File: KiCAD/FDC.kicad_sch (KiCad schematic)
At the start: 26 parts, among them J2 Conn_02x20_Odd_Even, J3 SD_Card, Q1 SSM3K324RLFCT-ND, Q2 SSM3K324RLFCT-ND, U1 SN74LVCC4245ADWR, U2 Pico 2, U3 SN74LVCC4245ADWR, U4 SN74LVCC4245ADWR, U5 SN74LVCC4245ADWR

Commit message: First upload of test board.
First upload of test board.
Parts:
- removed C4, C5, C6, C7, C8: 100nF, Capacitor_SMD:C_0805_2012Metric_Pad1.18x1.45mm_HandSolder, symbol Device:C
- removed D2: PMEG4010CEJ, Diode_SMD:D_SOD-323F, symbol Diode:PMEG4010CEJ
- removed J2: Conn_02x20_Odd_Even, Connector_PinSocket_2.54mm:PinSocket_2x20_P2.54mm_Vertical, symbol Connector_Generic:Conn_02x20_Odd_Even
- removed J3: SD_Card, Connector_Card:SD_Kyocera_145638009511859+, symbol Connector:SD_Card
- removed R2: 1k, Resistor_SMD:R_0805_2012Metric_Pad1.20x1.40mm_HandSolder, symbol Device:R_US
- removed U1, U3, U4, U5: SN74LVCC4245ADWR, Package_SO:SOIC-24W_7.5x15.4mm_P1.27mm, symbol Logic_LevelTranslator:SN74AVC8T245PW
- added J1: Conn_01x04, Connector_PinHeader_2.54mm:PinHeader_1x04_P2.54mm_Vertical, symbol Connector_Generic:Conn_01x04
- added R1: 1k, Resistor_SMD:R_0805_2012Metric_Pad1.20x1.40mm_HandSolder, symbol Device:R_US
- added SDCARD1: ST-TF-003A, 00-ProjectLib:MicroSD_Card_TB, symbol MicroSDCardSlot:ST-TF-003A
- added U1, U2, U3: 74HCT245, Package_SO:SOIC-20W_7.5x15.4mm_P1.27mm, symbol 74xx:74HC245
- added U6, U7: Z80, Package_DIP:DIP-40_W15.24mm, symbol CPU:Z84C00xxP
- D1: footprint LED_SMD:LED_2816_7142Metric_Pad3.20x4.45mm_HandSolder -> LED_THT:LED_D5.0mm
- PICO2: renamed from U2; footprint MCU_RaspberryPi_and_Boards:RPi_Pico_SMD_TH -> Module:RaspberryPi_Pico_SMD
- Q1, Q2: value SSM3K324RLFCT-ND -> 2N7002; Digikey SSM3K324RLFCT-ND -> 2N7002NTR-ND
- renumbered C9 to C4, R3 to R2, R4 to R3, R6 to R4, R8 to R5, R1 to R6
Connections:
- net RD' is gone; now on net RD*: PICO2.15 (GPIO11)
- net WR' is gone; now on net WR*: PICO2.16 (GPIO12)
- net +3V3: now also R2.1, SDCARD1.4 (VDD); no longer C1.1, C2.1, R2.2
- net +5V: now also C1.1, C2.1, R1.2, U1.20 (VCC), U2.1 (A->B), U2.20 (VCC), U3.1 (A->B), U3.20 (VCC), U6.11 (V_{CC}), U7.11 (V_{CC})
- net A0: now also U2.9 (A7), U6.30 (A_{0}), U7.30 (A_{0})
- net A1: now also U2.8 (A6), U6.31 (A_{1}), U7.31 (A_{1})
- net A10: now also U3.7 (A5), U6.40 (A_{10}), U7.40 (A_{10})
- net A11: now also U3.6 (A4), U6.1 (A_{11}), U7.1 (A_{11})
- net A12: now also U3.2 (A0), U6.2 (A_{12}), U7.2 (A_{12})
- net A13: now also U3.3 (A1), U6.3 (A_{13}), U7.3 (A_{13})
- net A14: now also U3.4 (A2), U6.4 (A_{14}), U7.4 (A_{14})
- net A15: now also U3.5 (A3), U6.5 (A_{15}), U7.5 (A_{15})
- net A2: now also U2.7 (A5), U6.32 (A_{2}), U7.32 (A_{2})
- net A3: now also U2.6 (A4), U6.33 (A_{3}), U7.33 (A_{3})
- net A4: now also U2.5 (A3), U6.34 (A_{4}), U7.34 (A_{4})
- net A5: now also U2.4 (A2), U6.35 (A_{5}), U7.35 (A_{5})
- net A6: now also U2.3 (A1), U6.36 (A_{6}), U7.36 (A_{6})
- net A7: now also U2.2 (A0), U6.37 (A_{7}), U7.37 (A_{7})
- net A8: now also U3.9 (A7), U6.38 (A_{8}), U7.38 (A_{8})
- net A9: now also U3.8 (A6), U6.39 (A_{9}), U7.39 (A_{9})
- net ADDRH_OE: now also U3.19 (CE)
- net ADDRL_OE: now also U2.19 (CE)
- net CD: now also SDCARD1.9 (CD)
- net CLK_SCLK: now also SDCARD1.5 (CLK)
- net CMD_MOSI: now also SDCARD1.3 (CMD)
- net D0: now also U1.3 (A1), U6.14 (D_{0}), U7.14 (D_{0})
- net D0': now also U1.17 (B1), U2.11 (B7), U3.11 (B7)
- net D1: now also U1.7 (A5), U6.15 (D_{1}), U7.15 (D_{1})
- net D1': now also U1.13 (B5), U2.12 (B6), U3.12 (B6)
- net D2: now also U1.2 (A0), U6.12 (D_{2}), U7.12 (D_{2})
- net D2': now also U1.18 (B0), U2.13 (B5), U3.13 (B5)
- net D3: now also U1.5 (A3), U6.8 (D_{3}), U7.8 (D_{3})
- net D3': now also U1.15 (B3), U2.14 (B4), U3.14 (B4)
- net D4: now also U1.9 (A7), U6.7 (D_{4}), U7.7 (D_{4})
- net D4': now also U1.11 (B7), U2.15 (B3), U3.18 (B0)
- net D5: now also U1.4 (A2), U6.9 (D_{5}), U7.9 (D_{5})
- net D5': now also U1.16 (B2), U2.16 (B2), U3.17 (B1)
- net D6: now also U1.6 (A4), U6.10 (D_{6}), U7.10 (D_{6})
- net D6': now also U1.14 (B4), U2.17 (B1), U3.16 (B2)
- net D7: now also U1.8 (A6), U6.13 (D_{7}), U7.13 (D_{7})
- net D7': now also U1.12 (B6), U2.18 (B0), U3.15 (B3)
- net DAT0_MISO: now also SDCARD1.7 (DAT0)
- net DAT3_CS: now also SDCARD1.2 (DAT3)
- net DATAB_OE: now also U1.19 (CE)
- net DIR: now also R1.1, U1.1 (A->B)
- net GND: now also SDCARD1.6 (VSS), SDCARD1.G1 (GND), SDCARD1.G2 (GND__1), SDCARD1.G3 (GND__2), SDCARD1.G4 (GND__3), U1.10 (GND), U2.10 (GND), U3.10 (GND), U6.29 (GND), U7.29 (GND); no longer PICO2.42 (GND)
- net IN': now also J1.1 (Pin_1)
- net INT*: now also U6.16 (~{INT}), U7.16 (~{INT})
- net MREQ': now also J1.3 (Pin_3)
- net OUT': now also J1.2 (Pin_2)
- net RD*: now also U6.21 (~{RD}), U7.21 (~{RD})
- net SYSRES': now also J1.4 (Pin_4)
- net WAIT*: now also U6.24 (~{WAIT}), U7.24 (~{WAIT})
- net WR*: now also U6.22 (~{WR}), U7.22 (~{WR})
- net at R3.1: now also SDCARD1.1 (DAT2)
- net SWCLK: no longer names the net of PICO2.41 (SWCLK)
- net SWDIO: no longer names the net of PICO2.43 (SWDIO)
- new net: R2.2, SDCARD1.8 (DAT1)
- new net BUSACK: U6.23 (~{BUSACK}), U7.23 (~{BUSACK})
- new net BUSREQ: U6.25 (~{BUSREQ}), U7.25 (~{BUSREQ})
- new net CLK: U6.6 (CLK), U7.6 (CLK)
- new net HALT: U6.18 (~{HALT}), U7.18 (~{HALT})
- new net IORQ: U6.20 (~{IORQ}), U7.20 (~{IORQ})
- new net M1: U6.27 (~{M1}), U7.27 (~{M1})
- new net MREQ: U6.19 (~{MREQ}), U7.19 (~{MREQ})
- new net NMI: U6.17 (~{NMI}), U7.17 (~{NMI})
- new net RESET: U6.26 (~{RESET}), U7.26 (~{RESET})
- new net RFSH: U6.28 (~{RFSH}), U7.28 (~{RFSH})
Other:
- moved on the sheet: C4, R2, R3

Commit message: New PCB.. this may fit
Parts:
- renumbered C3 to C1, C1 to C3
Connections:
- net IN': now also J1.2 (Pin_2); no longer J1.1 (Pin_1)
- net MREQ': now also J1.4 (Pin_4); no longer J1.3 (Pin_3)
- net OUT': now also J1.3 (Pin_3); no longer J1.2 (Pin_2)
- net SYSRES': now also J1.1 (Pin_1); no longer J1.4 (Pin_4)
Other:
- moved on the sheet: C1, C2, C3, C4, D1, J1, PICO2, Q1, Q2, R1, R2, R3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

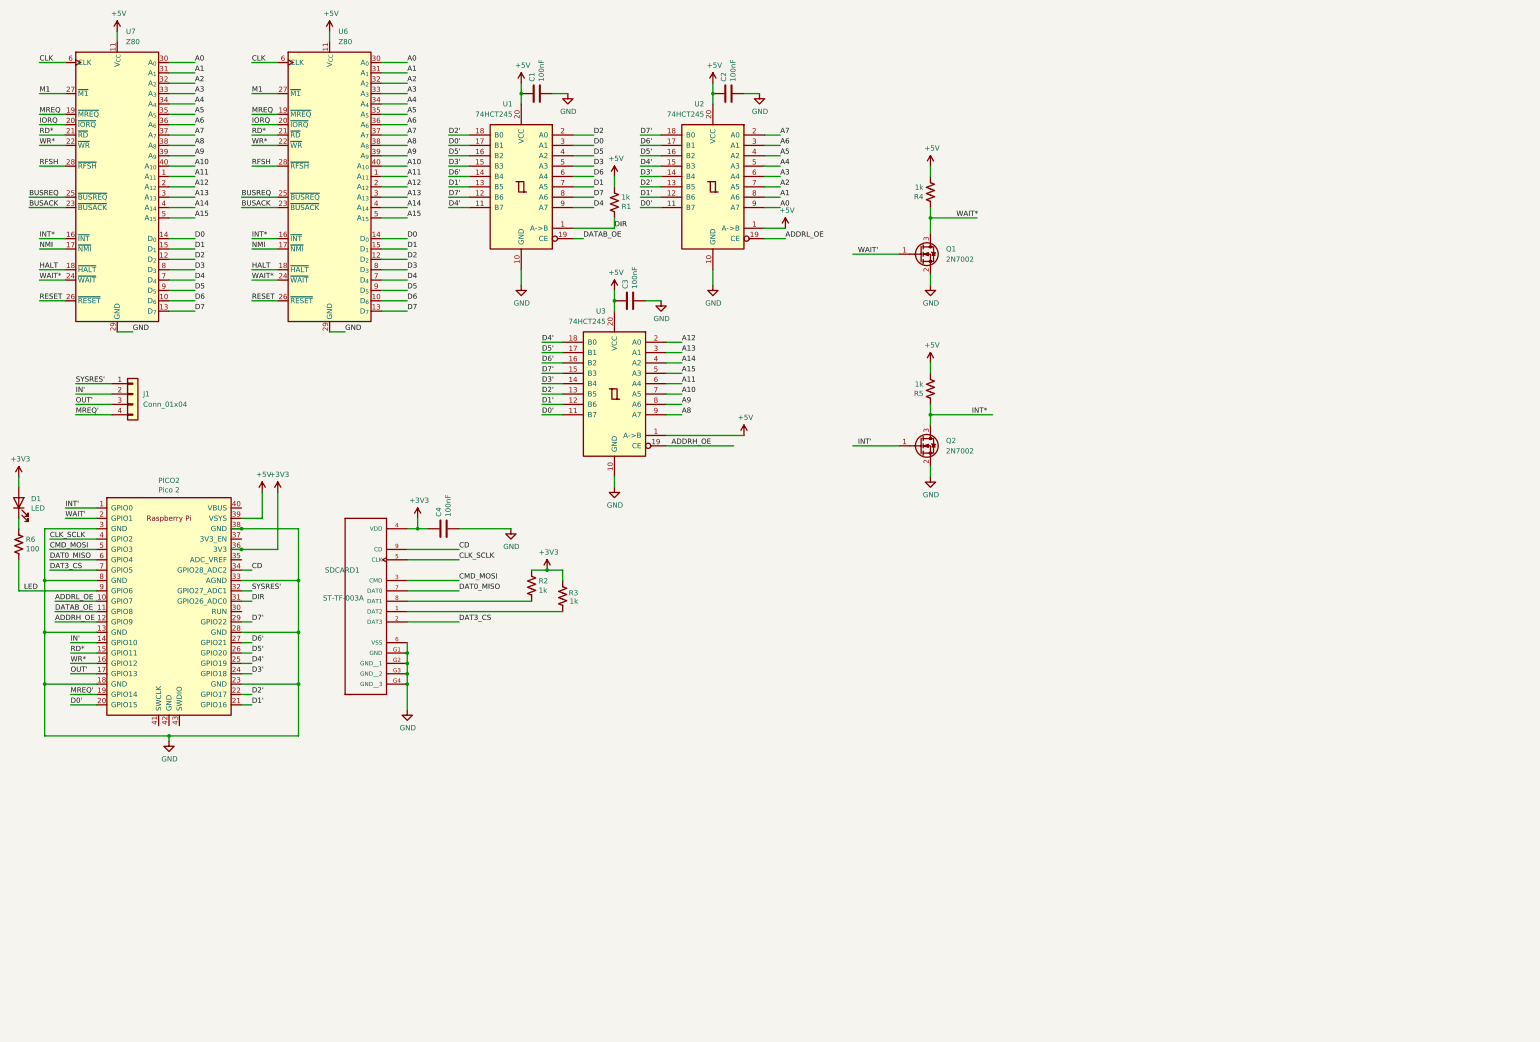
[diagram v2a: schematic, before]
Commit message: Updated PCB to ver 1.01
I didn't account for some signals on the first pcb.
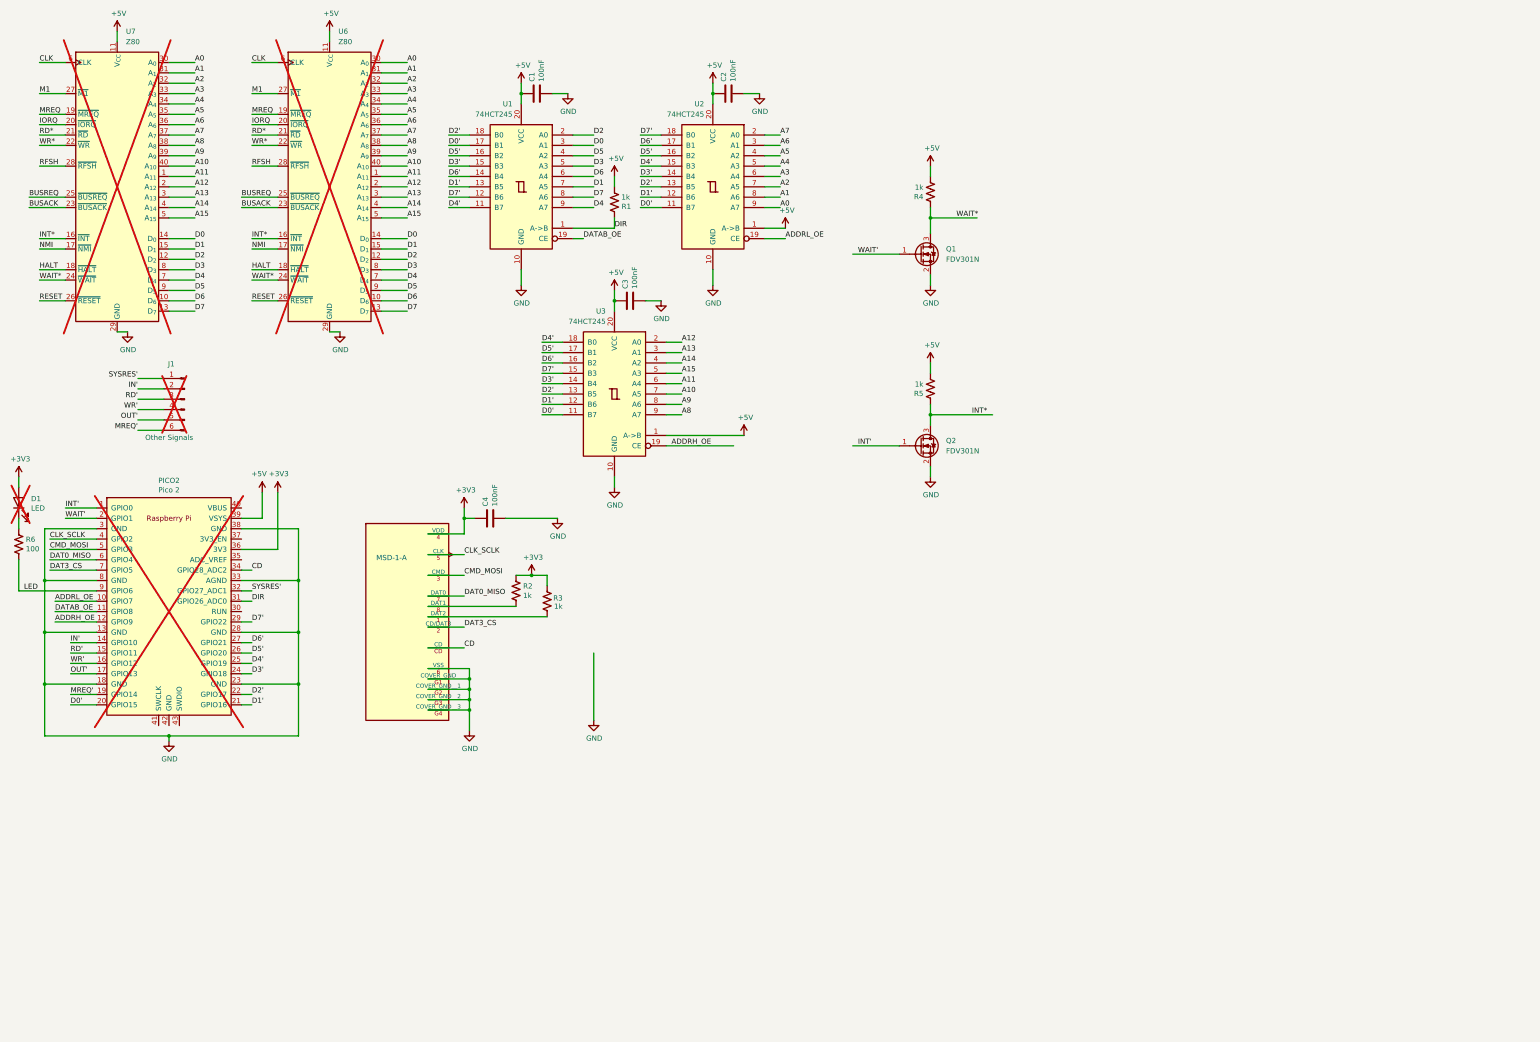
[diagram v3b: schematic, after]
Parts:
- removed J1: Conn_01x04, Connector_PinHeader_2.54mm:PinHeader_1x04_P2.54mm_Vertical, symbol Connector_Generic:Conn_01x04
- removed SDCARD1: ST-TF-003A, 00-ProjectLib:MicroSD_Card_TB, symbol MicroSDCardSlot:ST-TF-003A
- added J1: Other Signals, Connector_PinHeader_2.54mm:PinHeader_1x06_P2.54mm_Vertical, symbol Connector:Conn_01x06_Pin
- added SD1: MSD-1-A, SDCard:CUI_MSD-1-A, symbol SDcard:MSD-1-A
- C1, C2, C3: LCSC Part # (none) -> C49678
- C4: Cost 0.10 -> (none); LCSC Part # (none) -> C49678
- D1, PICO2, U6, U7: now not fitted; now left out of the parts list
- Q1, Q2: value 2N7002 -> FDV301N; Cost .37 -> (none); Digikey 2N7002NTR-ND -> FDV301NCT-ND; LCSC Part # (none) -> C15310
- R1, R2, R3, R4, R5: Cost 0.1 -> (none); LCSC Part # (none) -> C2907232
- R6: Cost 0.1 -> (none); LCSC Part # (none) -> C105577
- U1, U2, U3: Digikey (none) -> 74HCT245DCT-ND; LCSC Part # (none) -> C5979
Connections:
- net +3V3: now also SD1.4 (VDD)
- net CD: now also SD1.CD
- net CLK_SCLK: now also SD1.5 (CLK)
- net CMD_MOSI: now also SD1.3 (CMD)
- net DAT0_MISO: now also SD1.7 (DAT0)
- net DAT3_CS: now also SD1.2 (CD/DAT3)
- net GND: now also SD1.6 (VSS), SD1.G1 (COVER_GND), SD1.G2 (COVER_GND__1), SD1.G3 (COVER_GND__2), SD1.G4 (COVER_GND__3)
- net IN': now also J1.2 (Pin_2)
- net MREQ': now also J1.6 (Pin_6)
- net OUT': now also J1.5 (Pin_5)
- net RD*: no longer PICO2.15 (GPIO11)
- net SYSRES': now also J1.1 (Pin_1)
- net WR*: no longer PICO2.16 (GPIO12)
- net at R3.1: now also SD1.1 (DAT2)
- net at R2.2: now also SD1.8 (DAT1)
- new net RD': J1.3 (Pin_3), PICO2.15 (GPIO11)
- new net WR': J1.4 (Pin_4), PICO2.16 (GPIO12)
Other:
- moved on the sheet: C4, R2, R3

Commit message: New board revision
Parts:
- removed C1, C2, C3: 100nF, Capacitor_SMD:C_0805_2012Metric_Pad1.18x1.45mm_HandSolder, symbol Device:C
- removed J1: Other Signals, Connector_PinHeader_2.54mm:PinHeader_1x06_P2.54mm_Vertical, symbol Connector:Conn_01x06_Pin
- removed U1, U2, U3: 74HCT245, Package_SO:SOIC-20W_7.5x15.4mm_P1.27mm, symbol 74xx:74HC245
- added C23, C3-1, C3-2, C4, C5, C6, C7: 100nF, Capacitor_SMD:C_0805_2012Metric_Pad1.18x1.45mm_HandSolder, symbol Device:C
- added J1: Conn_01x01_Pin, Connector_PinHeader_2.54mm:PinHeader_1x01_P2.54mm_Vertical, symbol Connector:Conn_01x01_Pin
- added U23: SN74LS32NSR, Package_SO:SOIC-14_3.9x8.7mm_P1.27mm, symbol 74xx:74LS32
- added U3: SN74LVCC4245APWR, Package_SO:TSSOP-24_4.4x7.8mm_P0.65mm, symbol Logic_LevelTranslator:SN74AVC8T245PW
- added U4, U5, U6, U7: SN74LVC245APWR, Package_SO:TSSOP-20_4.4x6.5mm_P0.65mm, symbol 74LVC245:74LVC245
- renumbered C4 to C-SD1, U7 to U1, U6 to U2
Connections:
- net +3V3: now also R1.2, C3-2.2, C4.1, C5.1, C6.1, C7.1, U3.23 (VCCB), U3.24 (VCCB), U4.1 (DIR), U4.20 (VCC), U5.20 (VCC), U6.1 (DIR), U6.20 (VCC), U7.1 (DIR), U7.20 (VCC)
- net +5V: now also C23.1, C3-1.2, U23.14 (VCC), U3.1 (VCCA); no longer R1.2
- net A0: now also U4.9 (A8)
- net A1: now also U4.8 (A7)
- net A10: now also U6.7 (A6)
- net A11: now also U6.6 (A5)
- net A12: now also U6.2 (A1)
- net A13: now also U6.3 (A2)
- net A14: now also U6.4 (A3)
- net A15: now also U6.5 (A4)
- net A2: now also U4.7 (A6)
- net A3: now also U4.6 (A5)
- net A4: now also U4.5 (A4)
- net A5: now also U4.4 (A3)
- net A6: now also U4.3 (A2)
- net A7: now also U4.2 (A1)
- net A8: now also U6.9 (A8)
- net A9: now also U6.8 (A7)
- net ADDRH_OE: now also U6.19 (OE)
- net ADDRL_OE: now also U4.19 (OE)
- net D0: now also U3.4 (A2)
- net D0': now also U4.11 (B8), U5.17 (B2), U6.11 (B8)
- net D1: now also U3.8 (A6)
- net D1': now also U4.12 (B7), U5.13 (B6), U6.12 (B7)
- net D2: now also U3.3 (A1)
- net D2': now also U4.13 (B6), U5.18 (B1), U6.13 (B6)
- net D3: now also U3.6 (A4)
- net D3': now also U4.14 (B5), U5.15 (B4), U6.14 (B5)
- net D4: now also U3.10 (A8)
- net D4': now also U4.15 (B4), U5.11 (B8), U6.18 (B1)
- net D5: now also U3.5 (A3)
- net D5': now also U4.16 (B3), U5.16 (B3), U6.17 (B2)
- net D6: now also U3.7 (A5)
- net D6': now also U4.17 (B2), U5.14 (B5), U6.16 (B3)
- net D7: now also U3.9 (A7)
- net D7': now also U4.18 (B1), U5.12 (B7), U6.15 (B4)
- net DATAB_OE: now also U5.19 (OE)
- net DIR: now also U5.1 (DIR)
- net GND: now also C23.2, C3-1.1, C3-2.1, C4.2, C5.2, C6.2, C7.2, U23.7 (GND), U3.11 (GND), U3.12 (GND), U3.13 (GND), U3.22 (~{OE}), U4.10 (GND), U5.10 (GND), U6.10 (GND), U7.10 (GND), U7.19 (OE), U7.8 (A7), U7.9 (A8)
- net IN': now also U7.16 (B3)
- net IORQ: now also U23.10, U23.2
- net MREQ: now also U23.12, U23.4, U7.7 (A6)
- net MREQ': now also U7.13 (B6)
- net OUT': now also U7.18 (B1)
- net RD': now also U7.17 (B2)
- net RD*: now also U23.5, U23.9, U3.2 (DIR)
- net SYSRES': now also U7.14 (B5)
- net WR': now also U7.15 (B4)
- net WR*: now also U23.1, U23.13
- new net D0-: U3.20 (B2), U5.3 (A2)
- new net D1-: U3.16 (B6), U5.7 (A6)
- new net D2-: U3.21 (B1), U5.2 (A1)
- new net D3-: U3.18 (B4), U5.5 (A4)
- new net D4-: U3.14 (B8), U5.9 (A8)
- new net D5-: U3.19 (B3), U5.4 (A3)
- new net D6-: U3.17 (B5), U5.6 (A5)
- new net D7-: U3.15 (B7), U5.8 (A7)
- new net IN5V: U23.8, U7.4 (A3)
- new net OUT5V: U23.3, U7.2 (A1)
- new net RD5V: U23.6, U7.3 (A2)
- new net SYSRES*: J1.1 (Pin_1), U7.6 (A5)
- new net WR5V: U23.11, U7.5 (A4)
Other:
- title: (none) -> Floppy-M1-Internal
- moved on the sheet: Q1, Q2, R4, R5

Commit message: Dropped additional level shifter/corrected soic size.
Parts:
- removed C3-1, C3-2: 100nF, Capacitor_SMD:C_0805_2012Metric_Pad1.18x1.45mm_HandSolder, symbol Device:C
- removed U3: SN74LVCC4245APWR, Package_SO:TSSOP-24_4.4x7.8mm_P0.65mm, symbol Logic_LevelTranslator:SN74AVC8T245PW
- U5: renamed from U23; footprint Package_SO:SOIC-14_3.9x8.7mm_P1.27mm -> Package_SO:SO-14_5.3x10.2mm_P1.27mm
- renumbered C5 to C1, C6 to C2, C4 to C3, C7 to C4, C23 to C5, U5 to U1, U1 to U10, U2 to U11, U6 to U2, U4 to U3, U7 to U4
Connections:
- net D0- is gone; now on net D0: U1.3 (A2)
- net D1- is gone; now on net D1: U1.7 (A6)
- net D2- is gone; now on net D2: U1.2 (A1)
- net D3- is gone; now on net D3: U1.5 (A4)
- net D4- is gone; now on net D4: U1.9 (A8)
- net D5- is gone; now on net D5: U1.4 (A3)
- net D6- is gone; now on net D6: U1.6 (A5)
- net D7- is gone; now on net D7: U1.8 (A7)
